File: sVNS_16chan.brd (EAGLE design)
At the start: 37.9 x 25.1 mm, 56 parts, among them IC1 EFM8SB10F8G-A-CSP16R, IC2 OPA990IDCKR, J1 M50-3631042, J2 M50-3631042, J3 M50-3631042, U1 NT3H2211W0FHKH, U2 LT8410EDC-1#TRMPBF, U3 MUX36S16IRSNR, U4 MUX36S16IRSNR

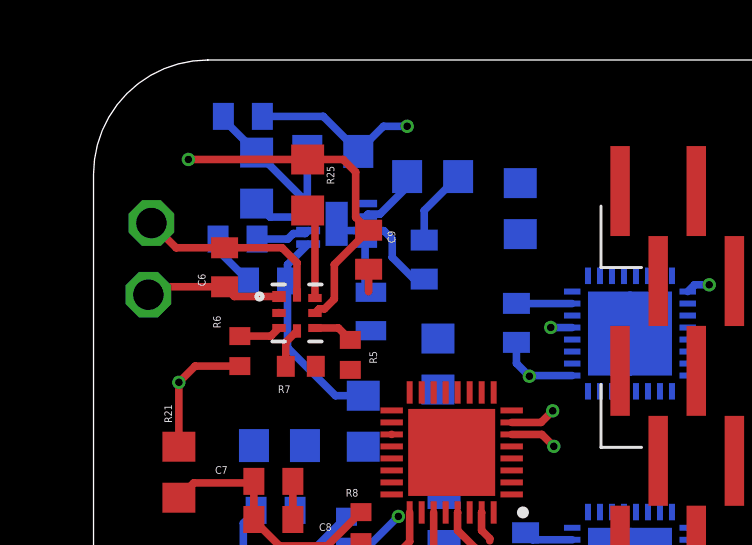
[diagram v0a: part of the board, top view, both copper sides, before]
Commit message: Power planes added. Ready for power pin assignment, routing and EFM8 package change
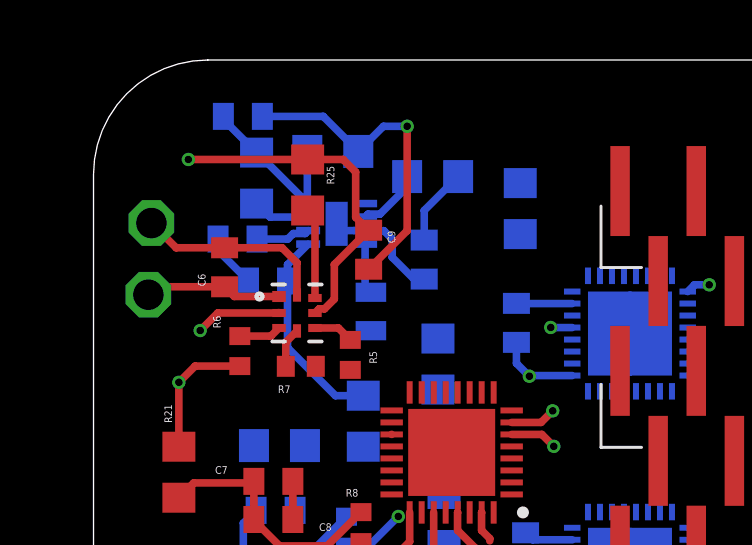
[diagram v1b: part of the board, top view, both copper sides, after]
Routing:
- net GND: track 30.1 -> 37.6 mm, vias 6 -> 7
- added copper zone on layer 15, net +20V
- added copper zone on layer 15, net +3.3V
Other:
- board text added: "+20V plane"
- board text added: "+3.3V plane"

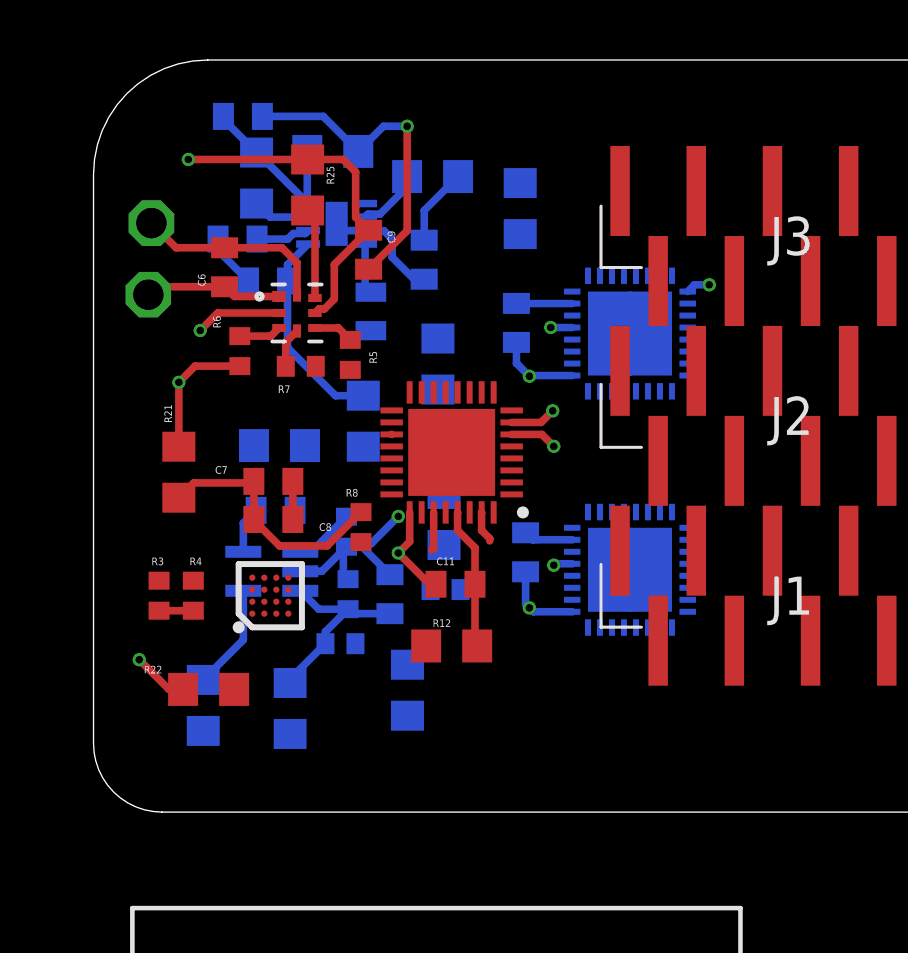
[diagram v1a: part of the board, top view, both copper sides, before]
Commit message: +3.3/+20V power pins assigned. Ready for control signal routing. Ready for MCU package change. Ready for MUXS16 rotaion
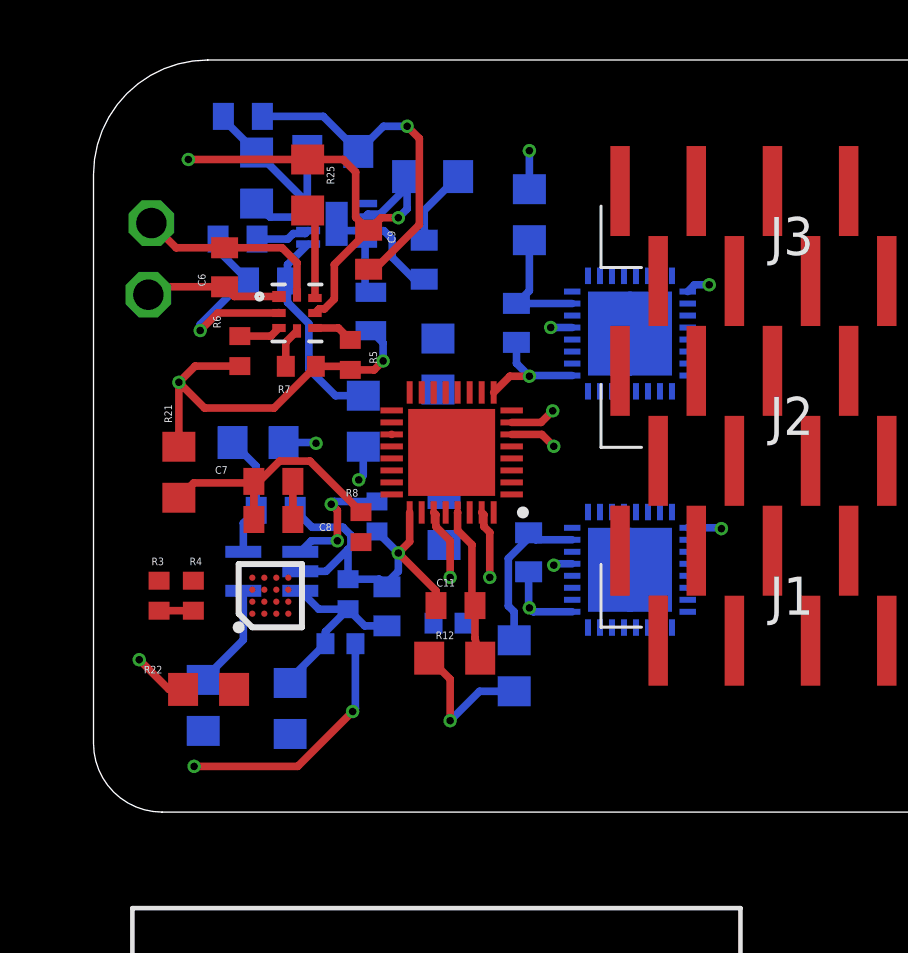
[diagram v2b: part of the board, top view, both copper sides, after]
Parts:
- moved R19 3.65 mm to (14.0, 4.88)
- moved R9 1.14 mm to (9.45, 9.86)
- moved R13 1.12 mm to (11.8, 6.30)
- moved R17 0.72 mm to (5.49, 12.3)
- moved C11 0.71 mm to (12.1, 6.88)
- moved C13 0.42 mm to (9.78, 6.86)
- moved R12 0.42 mm to (12.0, 5.13)
- moved R20 0.37 mm to (14.5, 19.9)
- moved C10 0.10 mm to (14.5, 8.66)
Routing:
- net +3.3V: track 18.1 -> 38.1 mm, vias 2 -> 6
- net GND: track 37.6 -> 46.3 mm
- net +20V: track 0.27 -> 8.77 mm, vias 0 -> 4
- net MUX36S16A+20V: track 1.69 -> 5.54 mm
- net P0.7_IREF: track 3.90 -> 6.49 mm, vias 1 -> 3
- net OPAMP_+20V: track 1.56 -> 4.14 mm
- net MUX36S16B_+20V: track 1.93 -> 4.22 mm
- net DB: track 1.06 -> 2.28 mm, vias 0 -> 1
- net DA: track 1.28 -> 2.39 mm, vias 0 -> 1

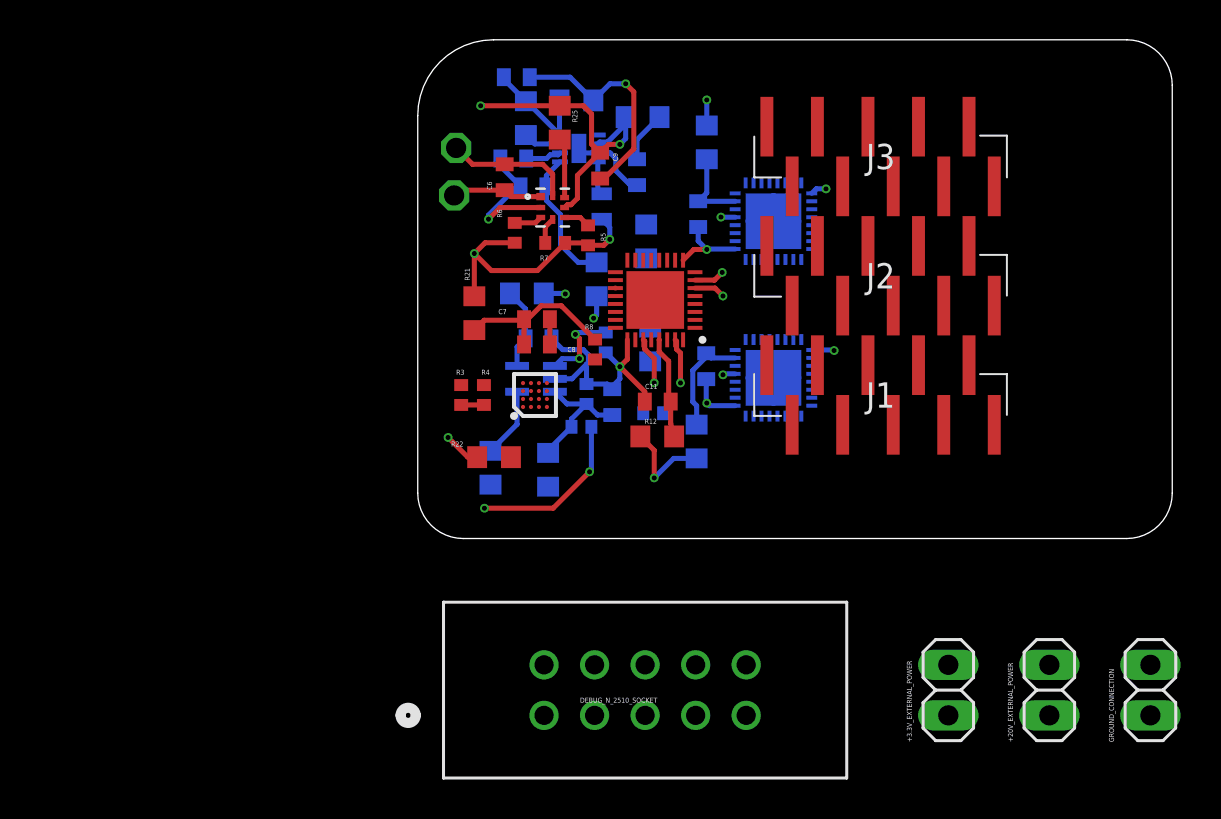
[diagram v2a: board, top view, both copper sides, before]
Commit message: Changed MCU package from CSP to QFN20. Ready to route signal traces. Ready for MUXS16 rotations
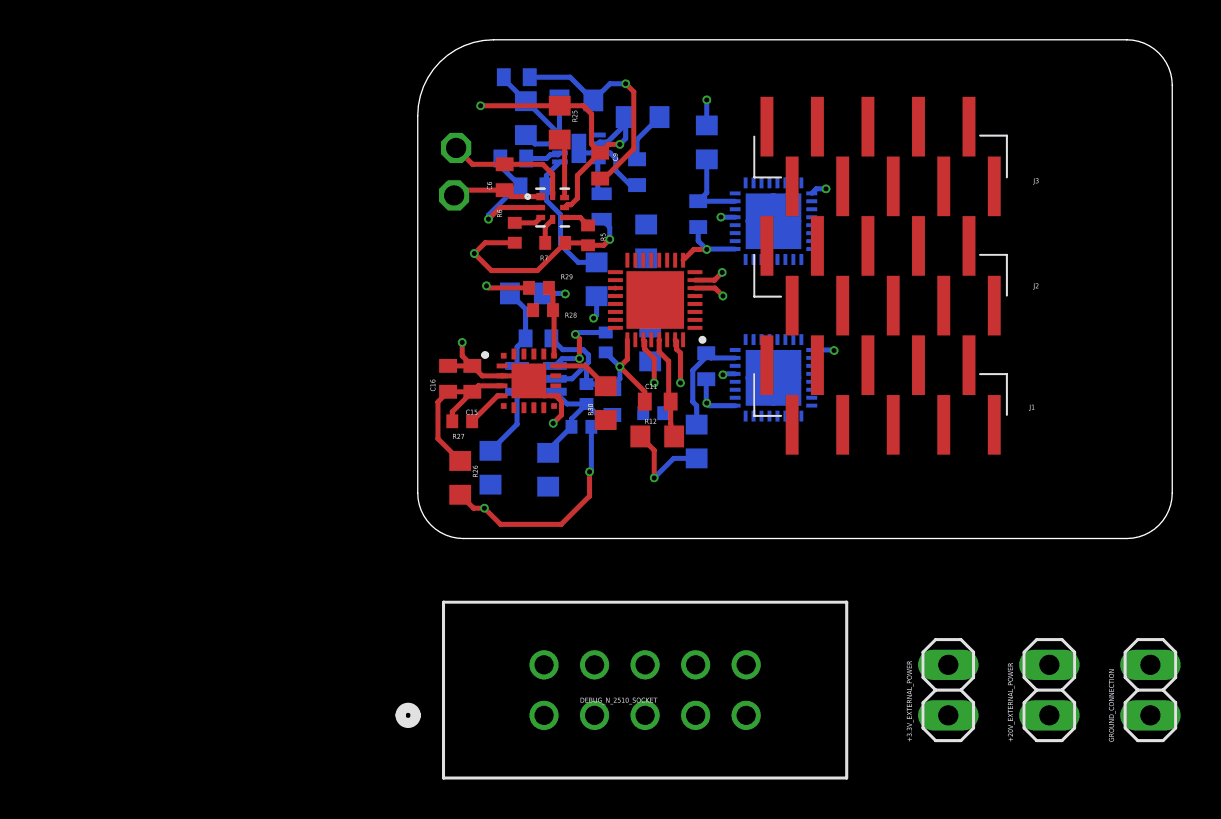
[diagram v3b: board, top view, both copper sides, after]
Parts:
- removed C7: 0.1 uF, rcl:C0402
- removed C8: 1 uF, rcl:C0402
- removed IC1: EFM8SB10F8G-A-CSP16R, sVNScomponents:BGA16C40P4X4_166X178X61
- removed R21, R22: (no value), sVNS_16chan_lib:R0603
- removed R3: 1.3M, rcl:R0402
- removed R4: 100k, rcl:R0402
- removed R8: 1k, rcl:R0402
- added C15: 0.1 uF, rcl:C0402
- added C16: 1 uF, rcl:C0402
- added IC3: EFM8SB10F2G-A-QFN20, SamacSys_Parts:EFM8SB10F8GAQFN20R
- added R26, R30: (no value), sVNS_16chan_lib:R0603
- added R27: 1k, rcl:R0402
- added R28: 100k, rcl:R0402
- added R29: 1.3M, rcl:R0402
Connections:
- net N$58 renamed CAP
- removed net FD: R7.1, U1.4
- removed net P0.0_SMBUS_SDA: IC1.A4, R5.1, U1.5
- removed net P0.1_A0_2: IC1.C3, U$1.15
- removed net P0.2_A1_1: IC1.B3, U3.14, U4.14
- removed net P0.3_A0_1: IC1.B2, U3.15, U4.15
- removed net P0.4_SMBUS_SCL: IC1.A3, R6.1, U1.3
- removed net P0.5_ADC: IC1.A2, R3.1, R4.2
- removed net P0.6_A3_1: IC1.C2, U3.10, U4.10
- removed net P0.7_IREF_PIN: IC1.A1, R22.2
- removed net P1.0_SHDN: IC1.B1, U$1.16, U2.1, U3.16, U4.16
- removed net P1.1_A1_2: IC1.D1, U$1.14
- removed net P1.3_A2_1: IC1.C1, U3.11, U4.11
- removed net P1.4_A2_2: IC1.D2, U$1.10
- new net P0.0_SMBUS0_SDA: IC3.2, R5.1, U1.5
- new net P0.1_SMBUS0_SCL: IC3.1, R6.1, U1.3
- new net P0.2_MUXD08_A0: IC3.20, U$1.15
- new net P0.3_MUXD08_A1: IC3.19, U$1.14
- new net P0.4_MUXD08_A2: IC3.18, U$1.10
- new net P0.5_SHDN: IC3.17, U$1.16, U2.1, U3.16, U4.16
- new net P0.6_ADC: IC3.16, R28.1, R29.2
- new net P1.0_FD: IC3.14, R7.1, U1.4
- new net P1.1: IC3.13
- new net P1.2: IC3.11
- new net P1.3_MUXS16_A0: IC3.10, U3.15, U4.15
- new net P1.5_MUXS16_A1: IC3.9, U3.14, U4.14
- new net P1.6_MUXS16_A2: IC3.8, U3.11, U4.11
- new net P1.7_MUXS16_A3: IC3.7, U3.10, U4.10
- net +3.3V: now also R26.2; no longer R21.2
- net +3.3V_VDD: now also C15.2, C16.1, IC3.4, R26.1, R27.2; no longer C7.2, C8.1, IC1.C4, R21.1, R8.1
- net GND: now also C15.1, C16.2, IC3.12, IC3.21, IC3.3, R28.2; no longer C7.1, C8.2, IC1.B4, R4.1
- net I_OUT+: now also R29.1; no longer R3.2
- net P0.7_IREF: now also IC3.15, R30.1, R30.2; no longer R22.1
- net P2.7_/_C2D: now also IC3.6; no longer IC1.D4
- net RSTB_/_C2CK: now also IC3.5, R27.1; no longer IC1.D3, R8.2
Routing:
- net GND: track 46.3 -> 56.3 mm, vias 7 -> 10
- net P0.6_ADC: track 0.00 -> 3.52 mm
- net RSTB_/_C2CK: track 0.00 -> 2.03 mm
- net P0.4_SMBUS_SCL: track 1.42 -> 0.00 mm
- net P0.1_SMBUS0_SCL: track 0.00 -> 1.42 mm
- net P0.0_SMBUS_SDA: track 1.34 -> 0.00 mm
- net P0.0_SMBUS0_SDA: track 0.00 -> 1.34 mm
- net P1.0_FD: track 0.00 -> 1.33 mm
- net FD: track 1.33 -> 0.00 mm
- net P0.5_ADC: track 1.14 -> 0.00 mm
- net P0.7_IREF: track 6.49 -> 7.55 mm, vias 3 -> 2
- net +3.3V: track 38.1 -> 38.9 mm

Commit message: Optimized component placement. Ready for signal routing. Ready for power/gnd vias.
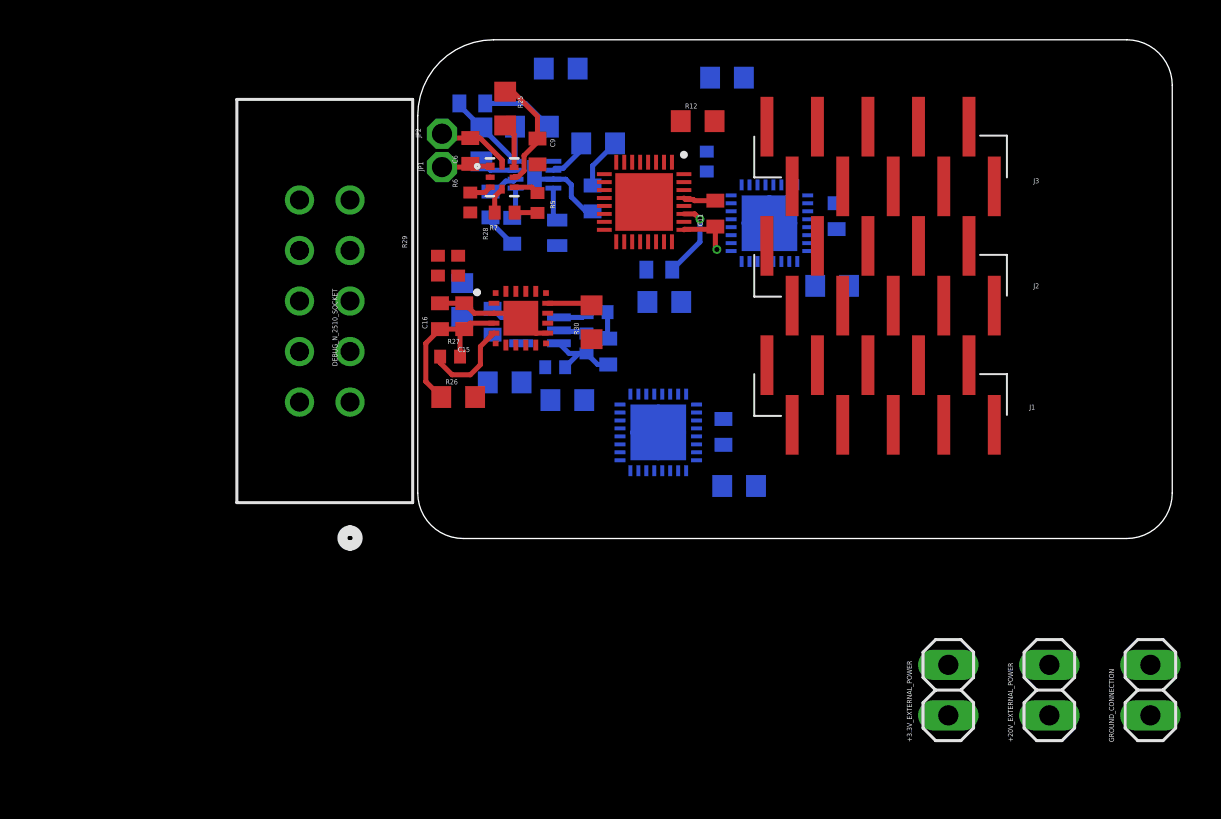
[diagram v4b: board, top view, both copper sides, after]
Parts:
- moved DEBUG_N_2510_SOCKET 18.5 mm to (-3.40, 6.86), turned to 90 degrees
- moved R12 16.0 mm to (14.1, 21.0)
- moved R14 14.0 mm to (15.5, 23.2), turned to 0 degrees
- moved R13 12.9 mm to (14.5, 18.9), turned to 90 degrees
- moved R24 10.7 mm to (7.19, 23.6), turned to 0 degrees
- moved C11 9.88 mm to (15.0, 16.3), turned to 90 degrees
- moved R20 9.58 mm to (20.8, 12.7), turned to 180 degrees
- moved R16 8.55 mm to (2.24, 12.0), turned to 90 degrees
- moved C5 6.96 mm to (21.1, 16.2), turned to 270 degrees
- moved U3 6.41 mm to (12.1, 5.33), turned to 90 degrees
- moved R29 5.74 mm to (1.02, 13.7), turned to 90 degrees
- moved U$1 4.96 mm to (11.4, 16.9), turned to 270 degrees
- moved R17 4.61 mm to (4.37, 7.85)
- moved R28 4.21 mm to (2.03, 13.7), turned to 270 degrees
- moved R30 4.13 mm to (8.74, 10.9)
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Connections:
- new net P0.7_IREF_PIN: IC3.15, R30.2
- net P0.7_IREF: no longer IC3.15, R30.2
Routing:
- net GND: track 56.3 -> 23.0 mm, vias 10 -> 1
- net +3.3V: track 38.9 -> 9.12 mm, vias 6 -> 0
- net +20V: track 8.77 -> 0.27 mm, vias 4 -> 0
- net P0.7_IREF: track 7.55 -> 1.56 mm, vias 2 -> 0
- net MUX36S16A+20V: track 5.54 -> 0.00 mm
- net +20V_PIN: track 7.03 -> 1.63 mm
- net MUX36S16B_+20V: track 4.22 -> 0.00 mm
- net I_OUT+_PIN: track 3.52 -> 0.00 mm
- net P0.6_ADC: track 3.52 -> 0.00 mm
- net MUX36D08_+20V: track 5.12 -> 1.71 mm
- net LB: track 6.47 -> 3.83 mm
- net RSTB_/_C2CK: track 2.03 -> 4.67 mm
- net OPAMP_+20V: track 4.14 -> 1.62 mm
- net I_OUT-_PIN: track 6.63 -> 4.28 mm
- net DB: track 2.28 -> 0.00 mm, vias 1 -> 0
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
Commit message: Routing half-done. Checkpoint 1
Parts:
- moved R9 4.21 mm to (7.92, 7.32)
- moved C13 4.21 mm to (8.46, 5.33)
- moved IC2 4.21 mm to (5.03, 6.40)
- moved R10 4.21 mm to (5.79, 4.55)
- moved R17 4.21 mm to (3.25, 3.78)
- moved R18 4.21 mm to (6.40, 2.90)
- moved C12 4.21 mm to (2.64, 6.83)
- moved R11 4.21 mm to (7.37, 5.74)
- moved R16 4.21 mm to (1.12, 7.92)
- moved C4 4.03 mm to (14.8, 10.5)
- moved R15 4.03 mm to (15.0, 8.84)
- moved C11 3.18 mm to (15.9, 13.3)
- moved U$1 3.18 mm to (12.3, 13.9)
- moved C10 1.72 mm to (16.6, 4.14)
- moved R19 1.72 mm to (17.4, 1.42)
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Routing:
- net P1.0_FD: track 1.33 -> 12.4 mm, vias 0 -> 2
- net P0.2_MUXD08_A0: track 0.00 -> 9.06 mm
- net P0.0_SMBUS0_SDA: track 1.30 -> 10.2 mm, vias 0 -> 2
- net P0.4_MUXD08_A2: track 0.00 -> 8.21 mm, vias 0 -> 2
- net P0.3_MUXD08_A1: track 0.00 -> 7.91 mm, vias 0 -> 2
- net P0.6_ADC: track 0.00 -> 7.52 mm, vias 0 -> 2
- net P0.1_SMBUS0_SCL: track 1.11 -> 7.91 mm, vias 0 -> 2
- net P0.5_SHDN: track 0.00 -> 5.49 mm, vias 0 -> 2
- net I_OUT+: track 0.00 -> 5.35 mm, vias 0 -> 1
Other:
- board size 37.9 x 25.1 mm -> 38.4 x 25.1 mm

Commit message: Checkpoint 2
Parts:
- moved DEBUG_N_2510_SOCKET 2.14 mm to (-5.54, 6.76)
- moved R27 2.09 mm to (2.13, 7.11), turned to 180 degrees
- moved R26 1.68 mm to (1.32, 8.64)
- moved R19 0.29 mm to (17.6, 1.63)
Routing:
- net I_OUT-: track 0.00 -> 11.5 mm, vias 0 -> 1
- net P1.7_MUXS16_A3: track 0.00 -> 11.2 mm, vias 0 -> 1
- net P1.6_MUXS16_A2: track 0.00 -> 10.3 mm, vias 0 -> 1
- net P1.5_MUXS16_A1: track 0.00 -> 9.48 mm, vias 0 -> 1
- net P1.3_MUXS16_A0: track 0.00 -> 8.26 mm, vias 0 -> 1
- net P2.7_/_C2D: track 0.00 -> 7.33 mm, vias 0 -> 2
- net I_OUT+_PIN: track 0.00 -> 5.08 mm
- net P0.7_IREF: track 1.56 -> 4.65 mm, vias 0 -> 1
- net I_OUT-_PIN: track 4.28 -> 6.24 mm
- net +3.3V_VDD: track 8.25 -> 6.31 mm, vias 0 -> 1
- net RSTB_/_C2CK: track 4.67 -> 3.72 mm
- net P0.5_SHDN: track 5.49 -> 6.30 mm, vias 2 -> 3
- net GND: track 23.0 -> 23.8 mm, vias 1 -> 2
